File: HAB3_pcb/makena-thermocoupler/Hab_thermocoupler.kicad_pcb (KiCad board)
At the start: 2 copper layers, 34.3 x 19 mm, 11 parts, among them J1 Conn_01x02_Male, J2 Conn_01x06_Female, U1 MAX31855

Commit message: added labels and made board have 4 layers
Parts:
- moved C1 2.54 mm to (157.5, 88.9)
- moved C2 2.54 mm to (171.4, 88.9)
- moved R1 2.54 mm to (169.7, 91.4)
- moved D1 2.54 mm to (174.0, 92.7)
- moved D2 2.54 mm to (174.0, 90.2)
- moved J1 2.54 mm to (151.1, 87.6)
- moved J2 2.54 mm to (177.8, 80.0)
- moved L1 2.54 mm to (155.4, 86.4)
- moved L2 2.54 mm to (155.4, 91.4)
- moved R2 2.54 mm to (173.2, 86.4)
- moved U1 2.54 mm to (163.8, 88.9)
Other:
- copper layers 2 -> 4
- board text added: "3v3"
- board text added: "CLK"
- board text added: "CS"
- board text added: "DO"
- board text added: "GND"
- board text added: "Red-"
- board text added: "Vin"
- board text added: "Yellow+"

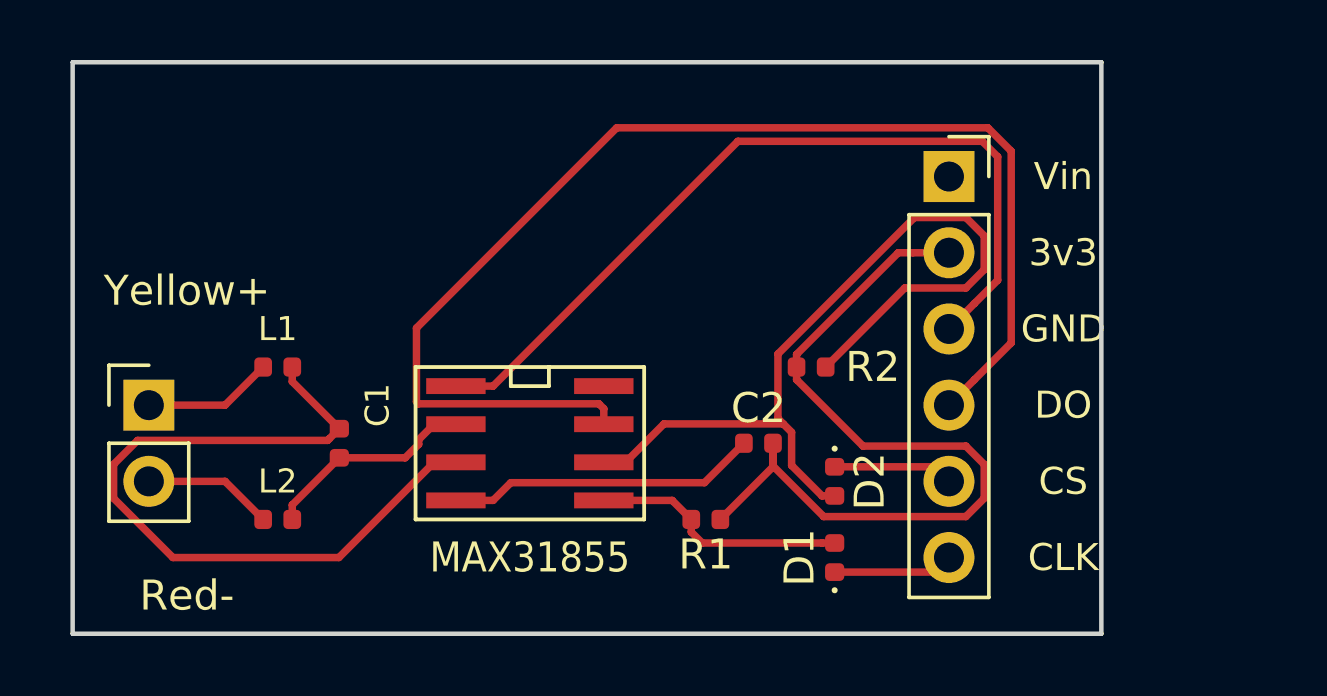
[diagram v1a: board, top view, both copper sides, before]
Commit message: changed diodes to be SOD 123 and updated footprint
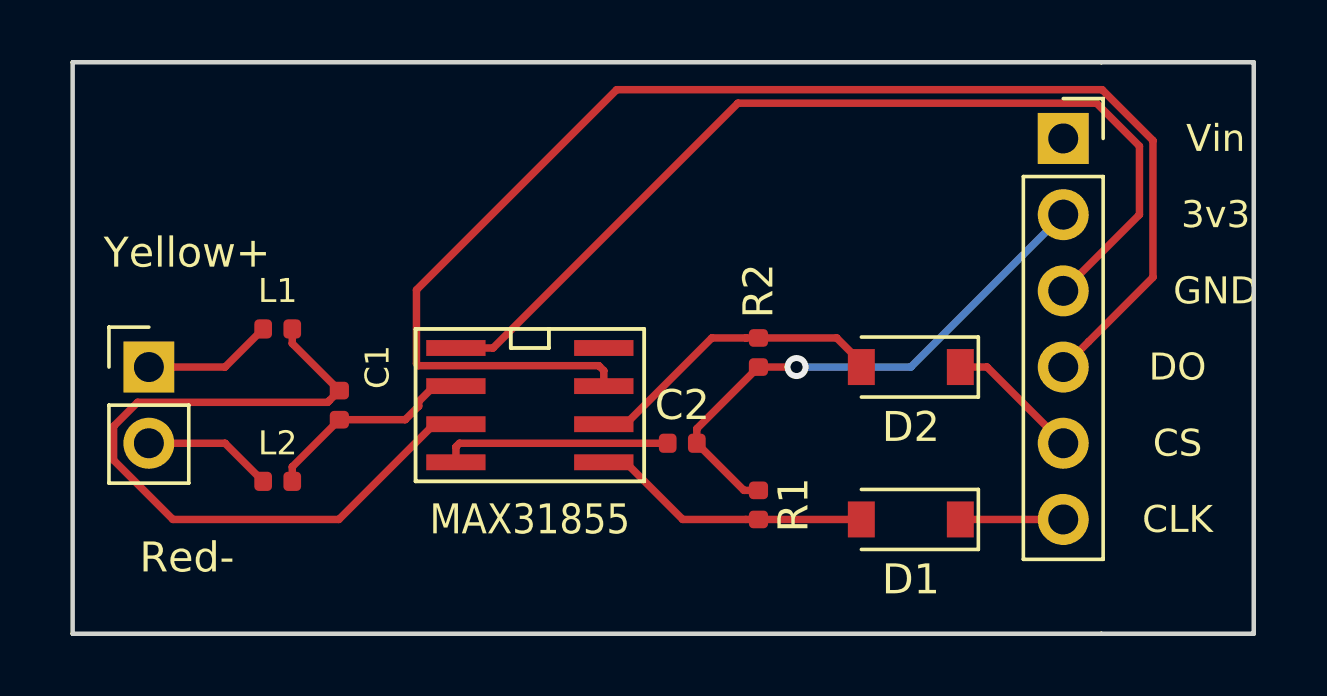
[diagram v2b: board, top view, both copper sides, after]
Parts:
- C1: value .01uF -> .01 uF
- C2: value 0.1uF -> 0.1 uF
- D1, D2: footprint Diode_SMD:D_0402_1005Metric -> Diode_SMD:D_SOD-123
- moved D2 4.58 mm to (176.5, 86.4), turned to 180 degrees
- moved J2 4.02 mm to (181.6, 78.7)
- moved D1 2.84 mm to (176.5, 91.4), turned to 180 degrees
- moved C2 2.54 mm to (168.9, 88.9)
- moved R2 1.82 mm to (171.4, 85.9), turned to 270 degrees
- moved R1 1.82 mm to (171.4, 91.0), turned to 270 degrees
- moved C1 1.27 mm to (157.5, 87.6)
- moved U1 1.27 mm to (163.8, 87.6)
- moved J1 1.27 mm to (151.1, 86.4)
- moved L1 1.27 mm to (155.4, 85.1)
- moved L2 1.27 mm to (155.4, 90.2)
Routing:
- net Net-(D2-Pad2): track 29.0 -> 10.3 mm
- net Net-(C2-Pad2): track 27.9 -> 18.4 mm, vias 0 -> 1
- net Net-(J2-Pad4): track 41.6 -> 46.1 mm
- net GND: track 28.1 -> 32.6 mm
- net Net-(C2-Pad1): track 10.4 -> 7.62 mm
- net Net-(D1-Pad2): track 8.53 -> 9.37 mm
- net Net-(D1-Pad1): track 4.01 -> 3.43 mm
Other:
- board size 34.3 x 19 mm -> 39.4 x 19 mm

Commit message: changed schematic and footprint following design review
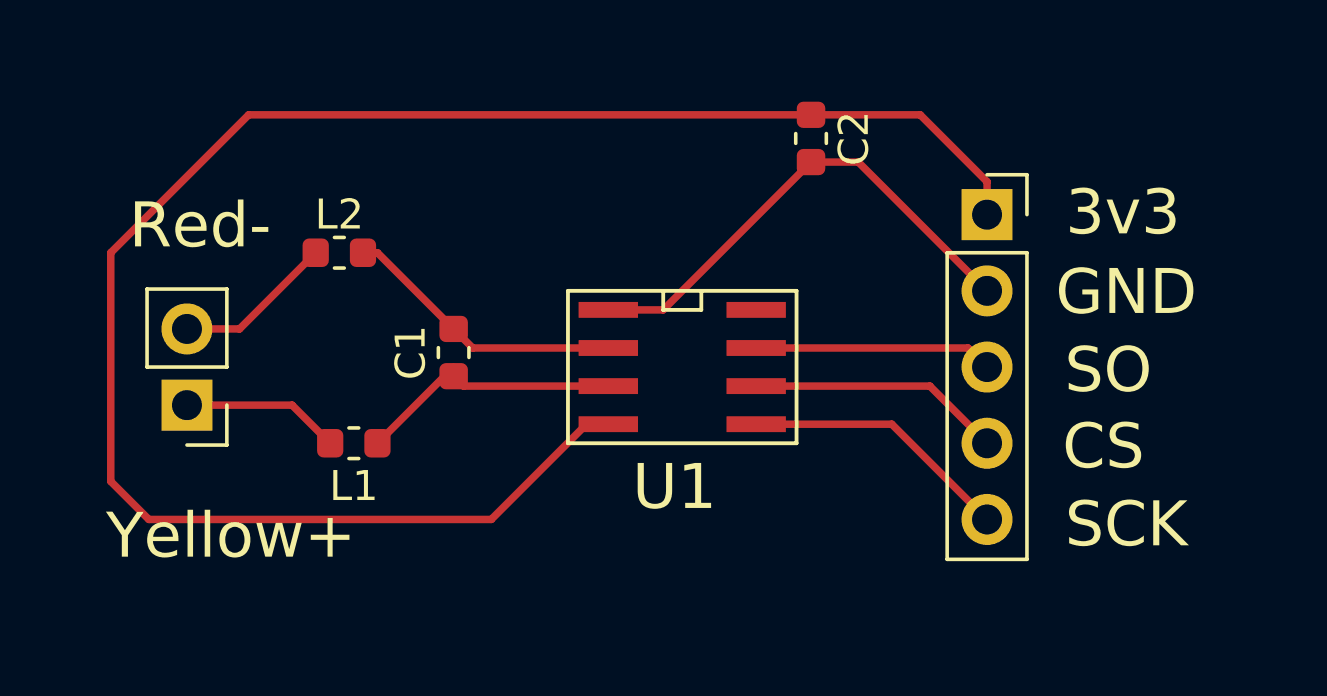
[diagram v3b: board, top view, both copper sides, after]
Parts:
- removed D1, D2: 1N4148, Diode_SMD:D_SOD-123
- removed R1, R2: 10k, Resistor_SMD:R_0402_1005Metric
- C1, C2: footprint Capacitor_SMD:C_0402_1005Metric -> Capacitor_SMD:C_0603_1608Metric
- J2: value Conn_01x06_Female -> Conn_01x05_Female; footprint Connector_PinSocket_2.54mm:PinSocket_1x06_P2.54mm_Vertical -> Connector_PinSocket_2.54mm:PinSocket_1x05_P2.54mm_Vertical
- L1, L2: footprint Inductor_SMD:L_0402_1005Metric -> Inductor_SMD:L_0603_1608Metric
- moved C2 11.0 mm to (173.2, 78.7), turned to 270 degrees
- moved L2 7.89 mm to (157.5, 82.5)
- moved U1 5.24 mm to (168.9, 86.4)
- moved L1 4.58 mm to (158.0, 88.9)
- moved C1 4.19 mm to (161.3, 85.9), turned to 90 degrees
- moved J2 3.59 mm to (179.1, 81.3)
- moved J1 1.80 mm to (152.4, 87.6), turned to 180 degrees
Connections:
- C2 pad 1: Net-(C2-Pad1) -> +3V3
- J2 pad 1: +5V -> +3V3
- J2 pad 3: GND -> Net-(J2-Pad3)
- J2 pad 5: Net-(D2-Pad1) -> Net-(J2-Pad5)
- U1 pad 1: GND -> Net-(C2-Pad2)
- U1 pad 4: Net-(C2-Pad1) -> +3V3
- U1 pad 5: Net-(D1-Pad2) -> Net-(J2-Pad5)
- U1 pad 6: Net-(D2-Pad2) -> Net-(J2-Pad4)
- U1 pad 7: Net-(J2-Pad4) -> Net-(J2-Pad3)
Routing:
- net +3V3: track 0.00 -> 59.2 mm
- net Net-(J2-Pad4): track 46.1 -> 8.48 mm
- net GND: track 32.6 -> 0.00 mm
- net Net-(C1-Pad1): track 25.4 -> 8.88 mm
- net Net-(D2-Pad2): track 10.3 -> 0.00 mm
- net Net-(D1-Pad2): track 9.37 -> 0.00 mm
- net Net-(J2-Pad5): track 0.00 -> 9.01 mm
- net Net-(J2-Pad3): track 0.00 -> 7.96 mm
- net Net-(C2-Pad1): track 7.62 -> 0.00 mm
- net Net-(D2-Pad1): track 4.48 -> 0.00 mm
- net Net-(D1-Pad1): track 3.43 -> 0.00 mm
- net Net-(C1-Pad2): track 7.15 -> 9.49 mm
- net Net-(C2-Pad2): track 18.4 -> 16.4 mm, vias 1 -> 0
- net Net-(J1-Pad2): track 4.34 -> 5.34 mm
- net Net-(J1-Pad1): track 4.34 -> 5.30 mm
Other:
- board outline removed
- board text added: "SCK"
- board text added: "SO"
- board text removed: "CLK"
- board text removed: "DO"
- board text removed: "Vin"

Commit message: changed footprints to be hand-soldered style
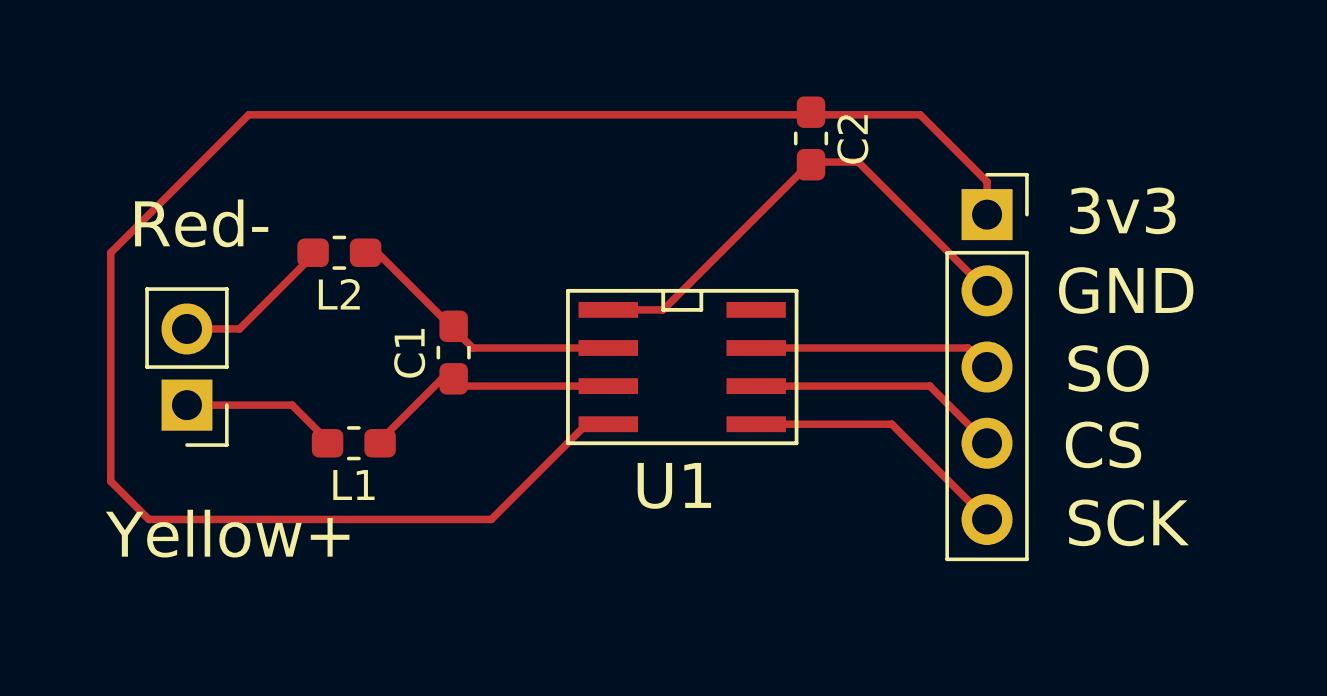
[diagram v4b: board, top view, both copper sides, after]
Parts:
- C1, C2: footprint Capacitor_SMD:C_0603_1608Metric -> Capacitor_SMD:C_0603_1608Metric_Pad1.05x0.95mm_HandSolder
- L1, L2: footprint Inductor_SMD:L_0603_1608Metric -> Inductor_SMD:L_0603_1608Metric_Pad1.05x0.95mm_HandSolder
